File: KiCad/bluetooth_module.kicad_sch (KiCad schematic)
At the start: 10 parts, among them U10 SN74LV1T34DCK, U11 RN4871, U12 LM810, U13 SN74LV1T34DCK, U9 SN74LV1T34DCK

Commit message: Create Revision 0.0.1
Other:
- company: (none) -> ETH Zurich: Center for Project Based Learning
- title: (none) -> STDC: Bluetooth Module
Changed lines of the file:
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@@
 	(generator_version "9.0")
 	(paper "A4")
+	(title_block
+		(title "STDC: Bluetooth Module")
+		(date "2026-03-05")
+		(rev "0.0.1")
+		(company "ETH Zurich: Center for Project Based Learning")
+	)
 	(rectangle
 		(start 57.15 19.05)

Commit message: Added some TODOs, fixed some TODOs
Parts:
- added C14, C57, C58, C59: 100n, Capacitor_SMD:C_0402_1005Metric, symbol Device:C
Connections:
- net +1V8: now also C14.1, C58.1
- net +3.3V: now also C57.1, C59.1
- net GND: now also C14.2, C57.2, C58.2, C59.2
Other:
- moved on the sheet: U9

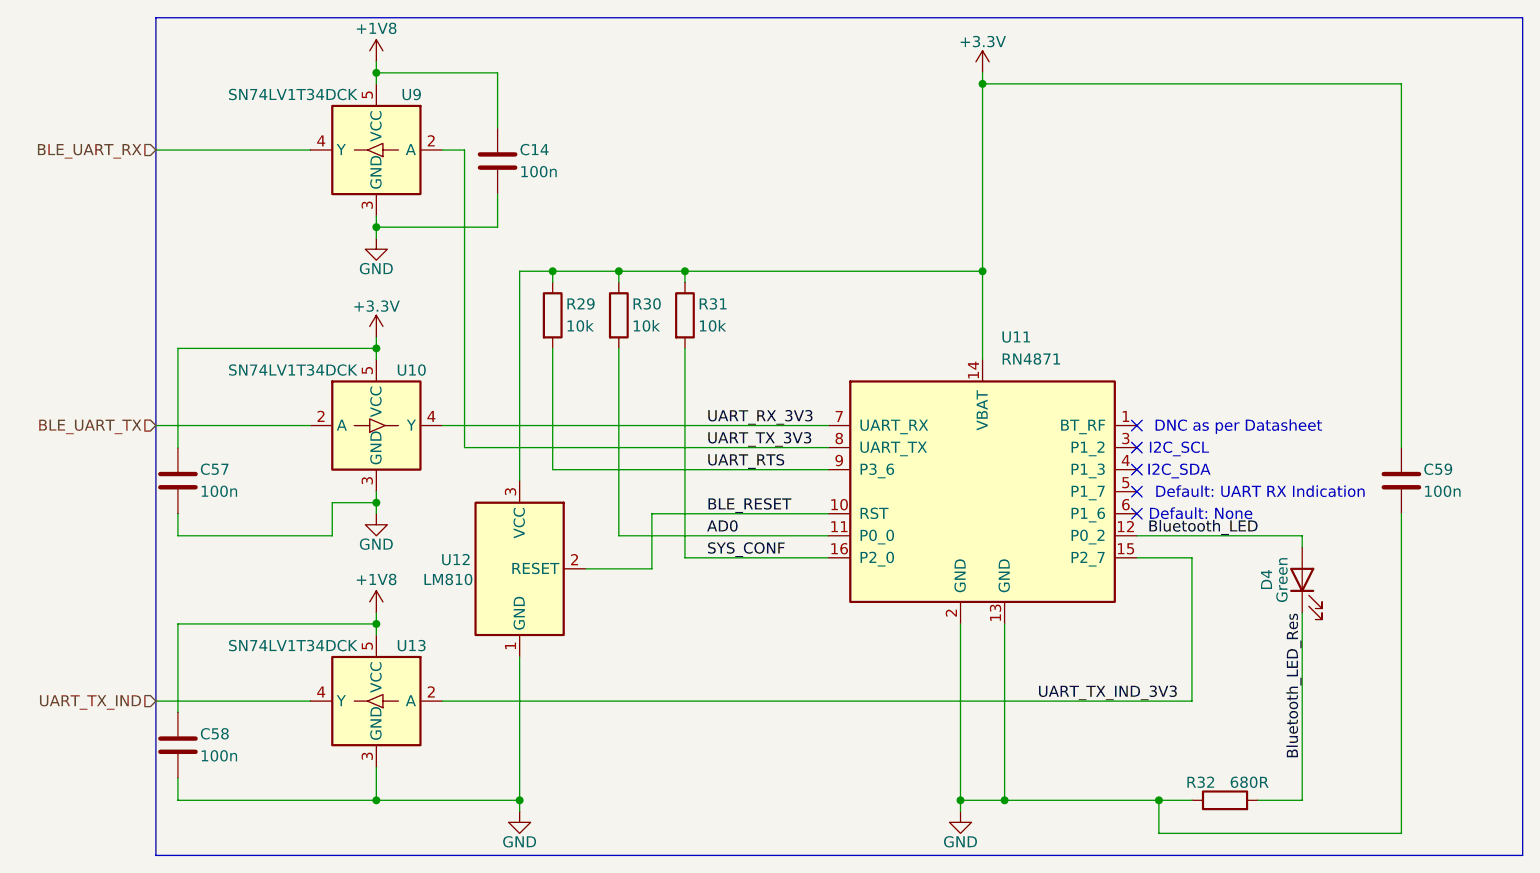
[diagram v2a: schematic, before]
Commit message: Testing connectors, SPI2 pinout, reannotate
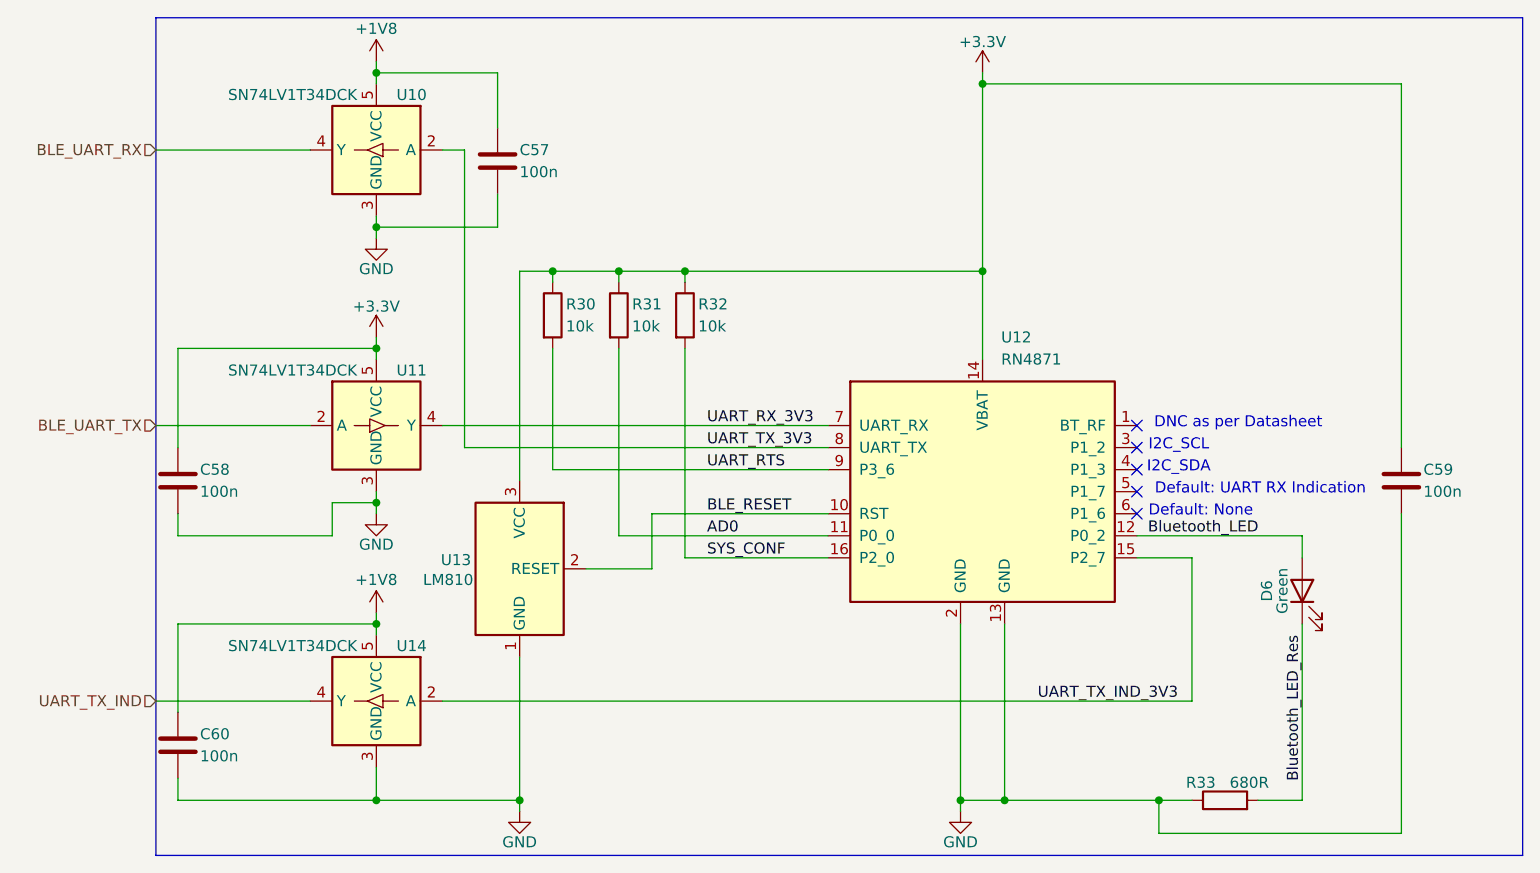
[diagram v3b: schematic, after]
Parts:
- renumbered C14 to C57, C57 to C58, C58 to C60, D4 to D6, R29 to R30, R30 to R31, R31 to R32, R32 to R33, U9 to U10, U10 to U11, U11 to U12, U12 to U13, U13 to U14
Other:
- moved on the sheet: D6

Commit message: Calculate saturation current for coils and add comments
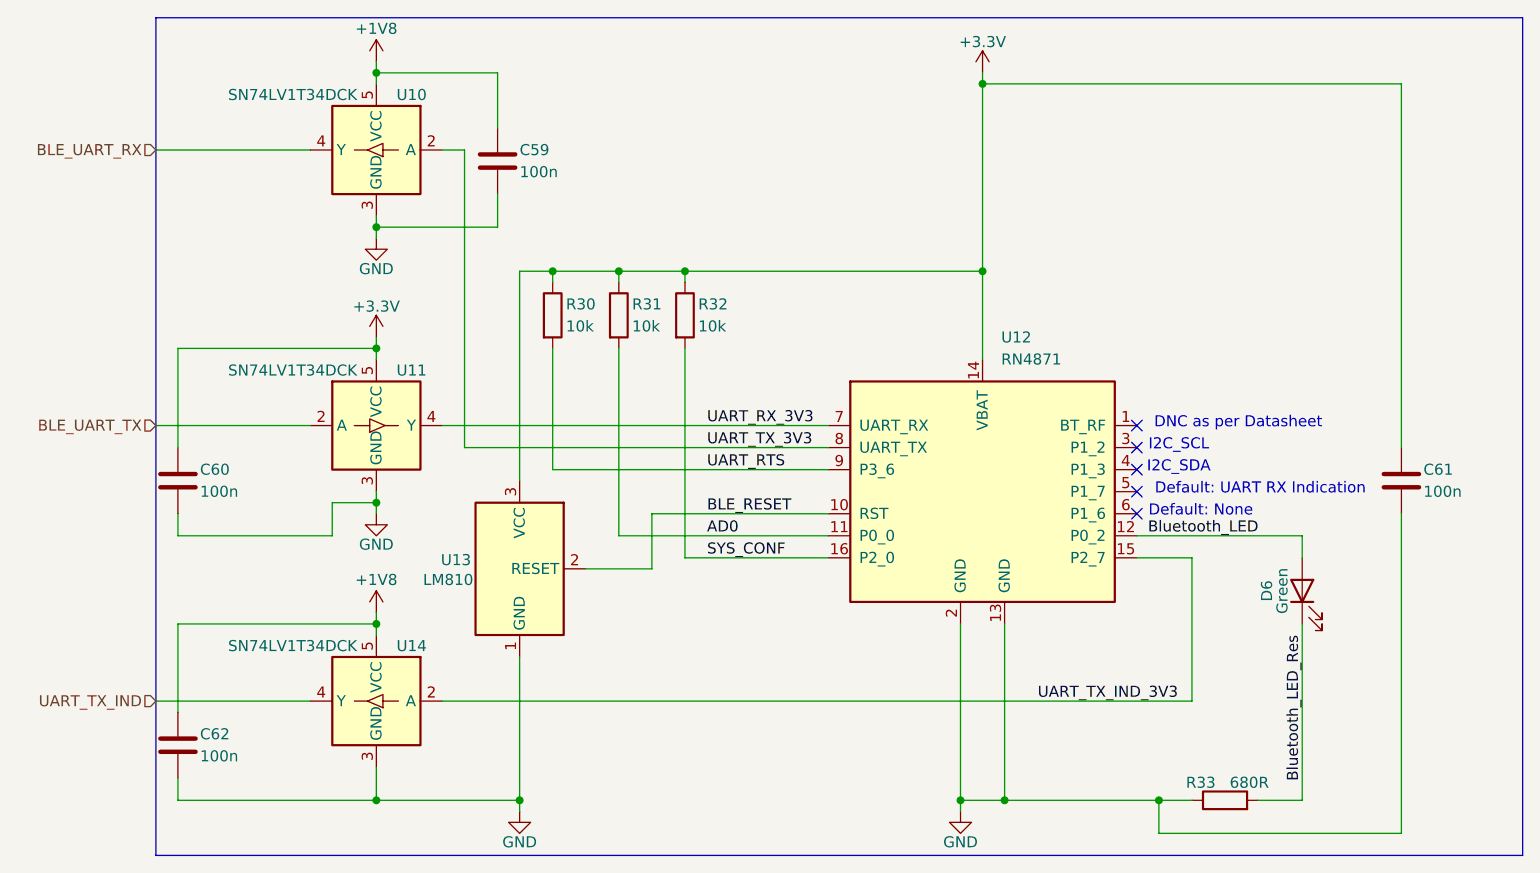
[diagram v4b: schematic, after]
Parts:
- renumbered C57 to C59, C58 to C60, C59 to C61, C60 to C62
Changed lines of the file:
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@@
 		(on_board yes)
 		(dnp no)
-		(property "Reference" "C59"
+		(property "Reference" "C61"
 			(at 199.39 67.31 0)
 			(effects
@@
 			(project "STDC"
 				(path "/643c756f-a801-466b-9148-7370ee6a5e00/ed1552c8-e376-430e-99d5-f81a0188f975"
-					(reference "C59")
+					(reference "C61")
 					(unit 1)
 				)
@@
 		(on_board yes)
 		(dnp no)
-		(property "Reference" "C58"
+		(property "Reference" "C60"
 			(at 58.42 67.31 0)
 			(effects
@@
 			(project "STDC"
 				(path "/643c756f-a801-466b-9148-7370ee6a5e00/ed1552c8-e376-430e-99d5-f81a0188f975"
-					(reference "C58")
+					(reference "C60")
 					(unit 1)
 				)
@@
 		(on_board yes)
 		(dnp no)
-		(property "Reference" "C57"
+		(property "Reference" "C59"
 			(at 95.25 30.48 0)
 			(effects
@@
 			(project "STDC"
 				(path "/643c756f-a801-466b-9148-7370ee6a5e00/ed1552c8-e376-430e-99d5-f81a0188f975"
-					(reference "C57")
+					(reference "C59")
 					(unit 1)
 				)
@@
 		(on_board yes)
 		(dnp no)
-		(property "Reference" "C60"
+		(property "Reference" "C62"
 			(at 58.42 97.79 0)
 			(effects
@@
 			(project "STDC"
 				(path "/643c756f-a801-466b-9148-7370ee6a5e00/ed1552c8-e376-430e-99d5-f81a0188f975"
-					(reference "C60")
-					(unit 1)
-				)
+					(reference "C62")
+					(unit 1)
+				)

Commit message: Add todos
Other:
- moved on the sheet: C60, C62
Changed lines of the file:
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@@
 	(wire
 		(pts
-			(xy 55.88 95.25) (xy 55.88 85.09)
+			(xy 57.15 95.25) (xy 57.15 85.09)
 		)
 		(stroke
@@
 	(wire
 		(pts
-			(xy 55.88 102.87) (xy 55.88 105.41)
-		)
-		(stroke
-			(width 0)
-			(type default)
-		)
-	)
-	(wire
-		(pts
-			(xy 55.88 105.41) (xy 78.74 105.41)
+			(xy 57.15 102.87) (xy 57.15 105.41)
+		)
+		(stroke
+			(width 0)
+			(type default)
+		)
+	)
+	(wire
+		(pts
+			(xy 57.15 105.41) (xy 78.74 105.41)
 		)
 		(stroke
@@
 	(wire
 		(pts
-			(xy 55.88 72.39) (xy 55.88 74.93)
+			(xy 57.15 72.39) (xy 57.15 74.93)
 		)
 		(stroke
@@
 	(wire
 		(pts
-			(xy 55.88 53.34) (xy 78.74 53.34)
+			(xy 57.15 53.34) (xy 78.74 53.34)
 		)
 		(stroke
@@
 	(wire
 		(pts
-			(xy 55.88 74.93) (xy 73.66 74.93)
+			(xy 57.15 74.93) (xy 73.66 74.93)
 		)
 		(stroke
@@
 	(wire
 		(pts
-			(xy 55.88 64.77) (xy 55.88 53.34)
+			(xy 57.15 64.77) (xy 57.15 53.34)
 		)
 		(stroke
@@
 	(wire
 		(pts
-			(xy 55.88 85.09) (xy 78.74 85.09)
+			(xy 57.15 85.09) (xy 78.74 85.09)
 		)
 		(stroke
@@
 	(symbol
 		(lib_id "Device:C")
-		(at 55.88 68.58 0)
+		(at 57.15 68.58 0)
 		(unit 1)
 		(exclude_from_sim no)
@@
 		(dnp no)
 		(property "Reference" "C60"
-			(at 58.42 67.31 0)
+			(at 59.69 67.31 0)
 			(effects
 				(font
@@
 		)
 		(property "Value" "100n"
-			(at 58.42 69.85 0)
+			(at 59.69 69.85 0)
 			(effects
 				(font
@@
 		)
 		(property "Footprint" "Capacitor_SMD:C_0402_1005Metric"
-			(at 56.8452 72.39 0)
+			(at 58.1152 72.39 0)
 			(effects
 				(font
@@
 		)
 		(property "Datasheet" "~"
-			(at 55.88 68.58 0)
+			(at 57.15 68.58 0)
 			(effects
 				(font
@@
 		)
 		(property "Description" "Unpolarized capacitor"
-			(at 55.88 68.58 0)
+			(at 57.15 68.58 0)
 			(effects
 				(font
@@
 	(symbol
 		(lib_id "Device:C")
-		(at 55.88 99.06 0)
+		(at 57.15 99.06 0)
 		(unit 1)
 		(exclude_from_sim no)
@@
 		(dnp no)
 		(property "Reference" "C62"
-			(at 58.42 97.79 0)
+			(at 59.69 97.79 0)
 			(effects
 				(font
@@
 		)
 		(property "Value" "100n"
-			(at 58.42 100.33 0)
+			(at 59.69 100.33 0)
 			(effects
 				(font
@@
 		)
 		(property "Footprint" "Capacitor_SMD:C_0402_1005Metric"
-			(at 56.8452 102.87 0)
+			(at 58.1152 102.87 0)
 			(effects
 				(font
@@
 		)
 		(property "Datasheet" "~"
-			(at 55.88 99.06 0)
+			(at 57.15 99.06 0)
 			(effects
 				(font
@@
 		)
 		(property "Description" "Unpolarized capacitor"
-			(at 55.88 99.06 0)
-			(effects
-				(font
+			(at 57.15 99.06 0)
+			(effects
+				(font

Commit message: First Draft PCB Layout
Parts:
- renumbered C59 to C56, C60 to C57, C61 to C58, C62 to C59, D6 to D4
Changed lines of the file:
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@@
 		(on_board yes)
 		(dnp no)
-		(property "Reference" "#PWR042"
+		(property "Reference" "#PWR039"
 			(at 78.74 78.74 0)
 			(effects
@@
 			(project "STDC"
 				(path "/643c756f-a801-466b-9148-7370ee6a5e00/ed1552c8-e376-430e-99d5-f81a0188f975"
-					(reference "#PWR042")
+					(reference "#PWR039")
 					(unit 1)
 				)
@@
 		(on_board yes)
 		(dnp no)
-		(property "Reference" "D6"
+		(property "Reference" "D4"
 			(at 181.356 81.28 0)
 			(effects
@@
 			(project "STDC"
 				(path "/643c756f-a801-466b-9148-7370ee6a5e00/ed1552c8-e376-430e-99d5-f81a0188f975"
-					(reference "D6")
+					(reference "D4")
 					(unit 1)
 				)
@@
 		(on_board yes)
 		(dnp no)
-		(property "Reference" "C61"
+		(property "Reference" "C58"
 			(at 199.39 67.31 0)
 			(effects
@@
 			(project "STDC"
 				(path "/643c756f-a801-466b-9148-7370ee6a5e00/ed1552c8-e376-430e-99d5-f81a0188f975"
-					(reference "C61")
+					(reference "C58")
 					(unit 1)
 				)
@@
 		(on_board yes)
 		(dnp no)
-		(property "Reference" "#PWR040"
+		(property "Reference" "#PWR037"
 			(at 78.74 46.99 0)
 			(effects
@@
 			(project "STDC"
 				(path "/643c756f-a801-466b-9148-7370ee6a5e00/ed1552c8-e376-430e-99d5-f81a0188f975"
-					(reference "#PWR040")
+					(reference "#PWR037")
 					(unit 1)
 				)
@@
 		(on_board yes)
 		(dnp no)
-		(property "Reference" "#PWR044"
+		(property "Reference" "#PWR041"
 			(at 95.25 113.03 0)
 			(effects
@@
 			(project "STDC"
 				(path "/643c756f-a801-466b-9148-7370ee6a5e00/ed1552c8-e376-430e-99d5-f81a0188f975"
-					(reference "#PWR044")
+					(reference "#PWR041")
 					(unit 1)
 				)
@@
 		(on_board yes)
 		(dnp no)
-		(property "Reference" "#PWR043"
+		(property "Reference" "#PWR040"
 			(at 78.74 87.63 0)
 			(effects
@@
 			(project "STDC"
 				(path "/643c756f-a801-466b-9148-7370ee6a5e00/ed1552c8-e376-430e-99d5-f81a0188f975"
-					(reference "#PWR043")
+					(reference "#PWR040")
 					(unit 1)
 				)
@@
 		(on_board yes)
 		(dnp no)
-		(property "Reference" "#PWR045"
+		(property "Reference" "#PWR042"
 			(at 146.05 113.03 0)
 			(effects
@@
 			(project ""
 				(path "/643c756f-a801-466b-9148-7370ee6a5e00/ed1552c8-e376-430e-99d5-f81a0188f975"
-					(reference "#PWR045")
+					(reference "#PWR042")
 					(unit 1)
 				)
@@
 		(on_board yes)
 		(dnp no)
-		(property "Reference" "#PWR038"
+		(property "Reference" "#PWR035"
 			(at 78.74 24.13 0)
 			(effects
@@
 			(project ""
 				(path "/643c756f-a801-466b-9148-7370ee6a5e00/ed1552c8-e376-430e-99d5-f81a0188f975"
-					(reference "#PWR038")
+					(reference "#PWR035")
 					(unit 1)
 				)
@@
 		(on_board yes)
 		(dnp no)
-		(property "Reference" "#PWR041"
+		(property "Reference" "#PWR038"
 			(at 78.74 55.88 0)
 			(effects
@@
 			(project "STDC"
 				(path "/643c756f-a801-466b-9148-7370ee6a5e00/ed1552c8-e376-430e-99d5-f81a0188f975"
-					(reference "#PWR041")
+					(reference "#PWR038")
 					(unit 1)
 				)
@@
 		(on_board yes)
 		(dnp no)
-		(property "Reference" "C60"
+		(property "Reference" "C57"
 			(at 59.69 67.31 0)
 			(effects
@@
 			(project "STDC"
 				(path "/643c756f-a801-466b-9148-7370ee6a5e00/ed1552c8-e376-430e-99d5-f81a0188f975"
-					(reference "C60")
+					(reference "C57")
 					(unit 1)
 				)
@@
 		(on_board yes)
 		(dnp no)
-		(property "Reference" "C59"
+		(property "Reference" "C56"
 			(at 95.25 30.48 0)
 			(effects
@@
 			(project "STDC"
 				(path "/643c756f-a801-466b-9148-7370ee6a5e00/ed1552c8-e376-430e-99d5-f81a0188f975"
-					(reference "C59")
+					(reference "C56")
 					(unit 1)
 				)
@@
 		(on_board yes)
 		(dnp no)
-		(property "Reference" "#PWR039"
+		(property "Reference" "#PWR036"
 			(at 148.59 25.4 0)
 			(effects
@@
 			(project ""
 				(path "/643c756f-a801-466b-9148-7370ee6a5e00/ed1552c8-e376-430e-99d5-f81a0188f975"
-					(reference "#PWR039")
+					(reference "#PWR036")
 					(unit 1)
 				)
@@
 		(on_board yes)
 		(dnp no)
-		(property "Reference" "C62"
+		(property "Reference" "C59"
 			(at 59.69 97.79 0)
 			(effects
@@
 			(project "STDC"
 				(path "/643c756f-a801-466b-9148-7370ee6a5e00/ed1552c8-e376-430e-99d5-f81a0188f975"
-					(reference "C62")
-					(unit 1)
-				)
+					(reference "C59")
+					(unit 1)
+				)

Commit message: Implement Comments, Working on PCB Layout
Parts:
- renumbered C56 to C53, C57 to C54, C58 to C55, C59 to C56, D4 to D6, R30 to R24, R31 to R25, R32 to R26, R33 to R27
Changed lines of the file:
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@@
 		(on_board yes)
 		(dnp no)
-		(property "Reference" "R30"
+		(property "Reference" "R24"
 			(at 100.584 48.26 0)
 			(effects
@@
 			(project "STDC"
 				(path "/643c756f-a801-466b-9148-7370ee6a5e00/ed1552c8-e376-430e-99d5-f81a0188f975"
-					(reference "R30")
+					(reference "R24")
 					(unit 1)
 				)
@@
 		(on_board yes)
 		(dnp no)
-		(property "Reference" "R32"
+		(property "Reference" "R26"
 			(at 115.824 48.26 0)
 			(effects
@@
 			(project ""
 				(path "/643c756f-a801-466b-9148-7370ee6a5e00/ed1552c8-e376-430e-99d5-f81a0188f975"
-					(reference "R32")
+					(reference "R26")
 					(unit 1)
 				)
@@
 		(on_board yes)
 		(dnp no)
-		(property "Reference" "D4"
+		(property "Reference" "D6"
 			(at 181.356 81.28 0)
 			(effects
@@
 			(project "STDC"
 				(path "/643c756f-a801-466b-9148-7370ee6a5e00/ed1552c8-e376-430e-99d5-f81a0188f975"
-					(reference "D4")
+					(reference "D6")
 					(unit 1)
 				)
@@
 		(on_board yes)
 		(dnp no)
-		(property "Reference" "C58"
+		(property "Reference" "C55"
 			(at 199.39 67.31 0)
 			(effects
@@
 			(project "STDC"
 				(path "/643c756f-a801-466b-9148-7370ee6a5e00/ed1552c8-e376-430e-99d5-f81a0188f975"
-					(reference "C58")
+					(reference "C55")
 					(unit 1)
 				)
@@
 		(on_board yes)
 		(dnp no)
-		(property "Reference" "C57"
+		(property "Reference" "C54"
 			(at 59.69 67.31 0)
 			(effects
@@
 			(project "STDC"
 				(path "/643c756f-a801-466b-9148-7370ee6a5e00/ed1552c8-e376-430e-99d5-f81a0188f975"
-					(reference "C57")
+					(reference "C54")
 					(unit 1)
 				)
@@
 		(on_board yes)
 		(dnp no)
-		(property "Reference" "C56"
+		(property "Reference" "C53"
 			(at 95.25 30.48 0)
 			(effects
@@
 			(project "STDC"
 				(path "/643c756f-a801-466b-9148-7370ee6a5e00/ed1552c8-e376-430e-99d5-f81a0188f975"
-					(reference "C56")
+					(reference "C53")
 					(unit 1)
 				)
@@
 		(on_board yes)
 		(dnp no)
-		(property "Reference" "C59"
+		(property "Reference" "C56"
 			(at 59.69 97.79 0)
 			(effects
@@
 			(project "STDC"
 				(path "/643c756f-a801-466b-9148-7370ee6a5e00/ed1552c8-e376-430e-99d5-f81a0188f975"
-					(reference "C59")
+					(reference "C56")
 					(unit 1)
 				)
@@
 		(on_board yes)
 		(dnp no)
-		(property "Reference" "R31"
+		(property "Reference" "R25"
 			(at 108.204 48.26 0)
 			(effects
@@
 			(project "STDC"
 				(path "/643c756f-a801-466b-9148-7370ee6a5e00/ed1552c8-e376-430e-99d5-f81a0188f975"
-					(reference "R31")
+					(reference "R25")
 					(unit 1)
 				)
@@
 		(on_board yes)
 		(dnp no)
-		(property "Reference" "R33"
+		(property "Reference" "R27"
 			(at 173.736 103.378 90)
 			(effects
@@
 			(project "STDC"
 				(path "/643c756f-a801-466b-9148-7370ee6a5e00/ed1552c8-e376-430e-99d5-f81a0188f975"
-					(reference "R33")
-					(unit 1)
-				)
+					(reference "R27")
+					(unit 1)
+				)
